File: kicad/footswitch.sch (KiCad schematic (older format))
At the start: 64 parts

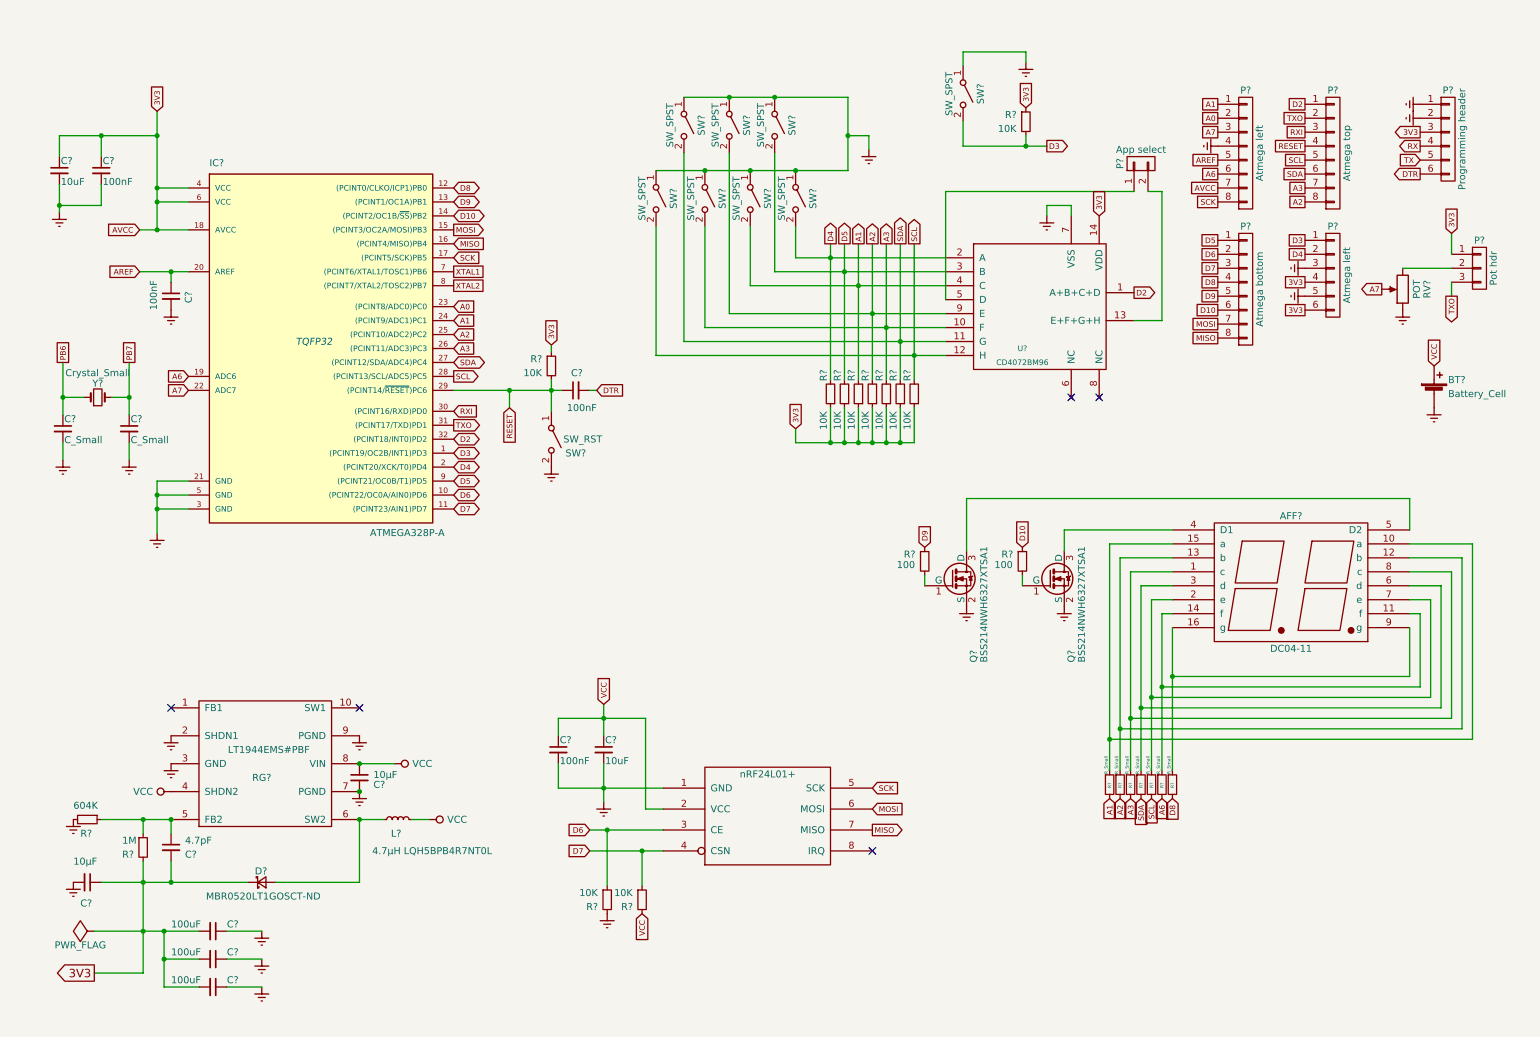
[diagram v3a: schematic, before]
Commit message: Finished schematic
- finished schematic drawing
- added schematic library for ldd-c514ri led display
- added footprint for 100SP4T1B1M1QEH mom-off-mom switch
- annotated footprints for components
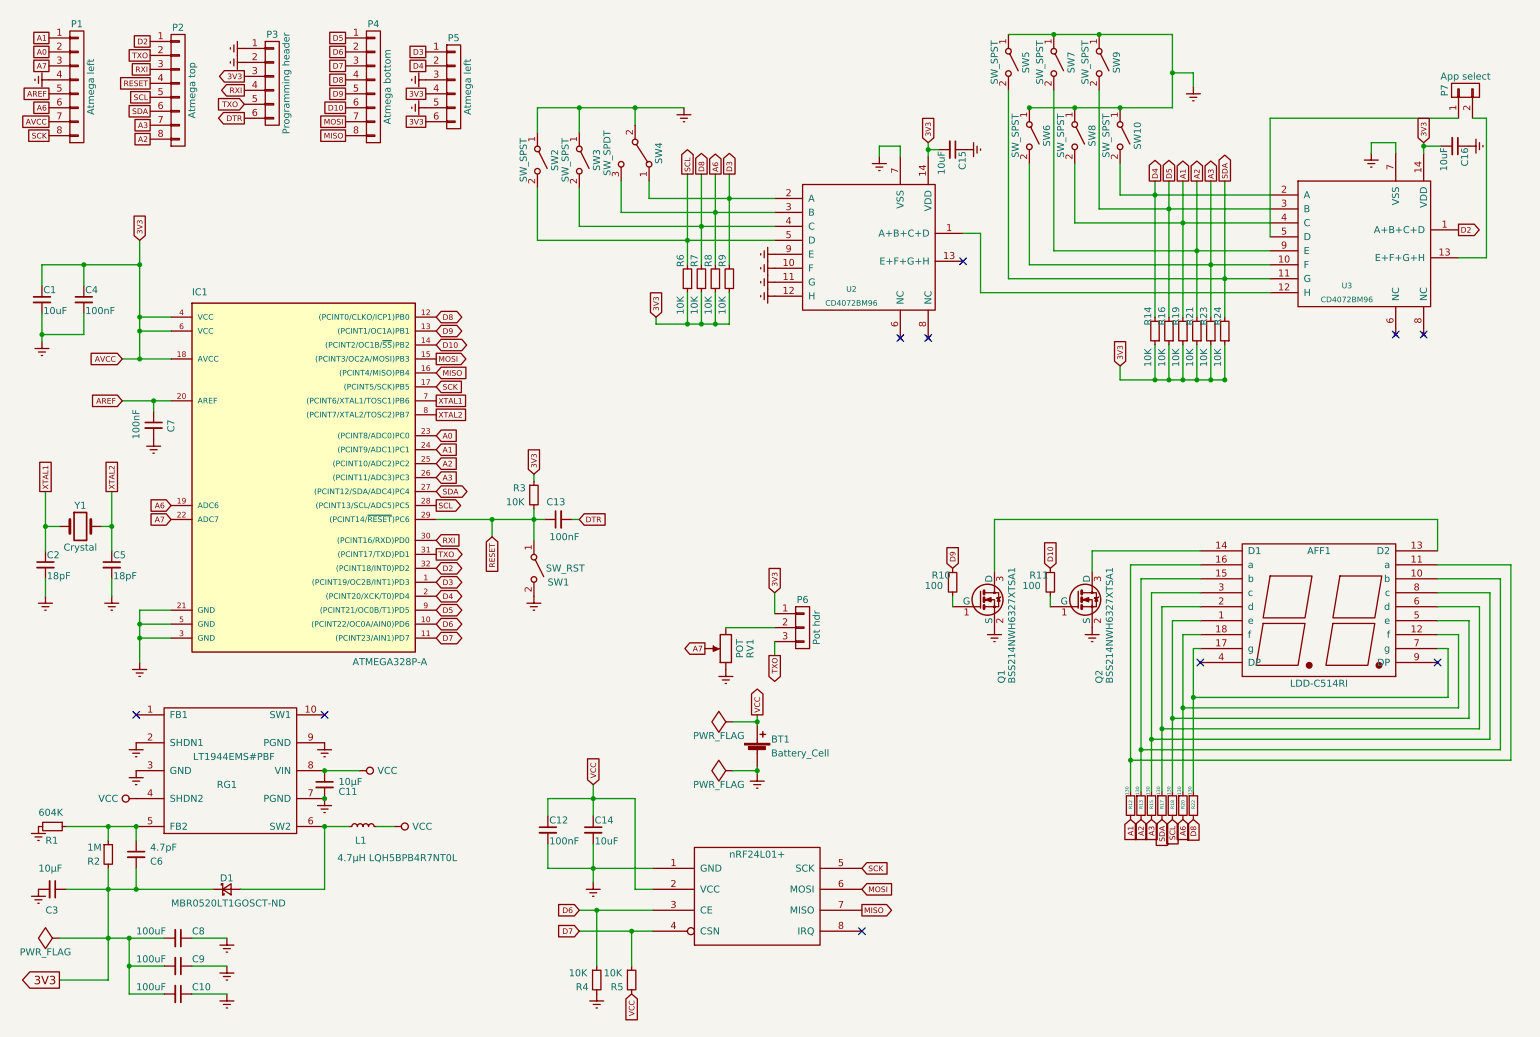
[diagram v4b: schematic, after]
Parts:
- removed AFF?: DC04-11, symbol DC04-11
- removed C? (x2): C_Small, symbol C_Small
- removed R?: 10K, symbol R_Small
- removed R?: 10K, Resistors_SMD:R_0805_HandSoldering, symbol R_Small
- removed Y?: Crystal_Small, symbol Crystal_Small
- added AFF1: LDD-C514RI, Displays_7-Segment:DA56, symbol LDD-C514RI
- added C15, C16: 10uF, Capacitors_SMD:C_1206_HandSoldering, symbol C_Small
- added C2, C5: 18pF, Capacitors_SMD:C_1206_HandSoldering, symbol C_Small
- added R6, R7, R8, R9: 10K, Resistors_SMD:R_1206_HandSoldering, symbol R_Small
- added SW4: SW_SPDT, switches:100SP4T1B1M1QEH, symbol SW_SPDT
- added U2: CD4072BM96, Housings_SOIC:SOIC-14_3.9x8.7mm_Pitch1.27mm, symbol CD4072BM96
- added Y1: Crystal, Crystals:Crystal_SMD_Abracon_ABM3-2pin_5.0x3.2mm_HandSoldering, symbol Crystal
- BT1: renamed from BT?; footprint (none) -> BC2AAPC:BC2AAPC
- C1, C12, C13, C14, C4, C7: renamed from C?; footprint (none) -> Capacitors_SMD:C_1206_HandSoldering
- C11, C3, C6: renamed from C?; footprint Capacitors_SMD:C_0805_HandSoldering -> Capacitors_SMD:C_1206_HandSoldering
- D1: renamed from D?; footprint Diodes_SMD:SOD-123 -> Diodes_SMD:D_SOD-123
- IC1: renamed from IC?; footprint TQFP32 -> Housings_QFP:TQFP-32_7x7mm_Pitch0.8mm
- L1: renamed from L?; footprint (none) -> Inductors:Inductor_Taiyo-Yuden_NR-50xx_HandSoldering
- P1, P2, P4: renamed from P?; footprint (none) -> Pin_Headers:Pin_Header_Straight_1x08_Pitch2.54mm
- P3, P5: renamed from P?; footprint (none) -> Pin_Headers:Pin_Header_Straight_1x06_Pitch2.54mm
- P6: renamed from P?; footprint (none) -> Pin_Headers:Pin_Header_Straight_1x03_Pitch2.54mm
- P7: renamed from P?; footprint (none) -> Pin_Headers:Pin_Header_Straight_1x02_Pitch2.54mm
- Q1, Q2: renamed from Q?; footprint TO_SOT_Packages_SMD:SOT-23 -> TO_SOT_Packages_SMD:SOT-323_SC-70_Handsoldering
- R1, R14, R16, R19, R2, R21, R23, R24, R4, R5: renamed from R?; footprint Resistors_SMD:R_0805_HandSoldering -> Resistors_SMD:R_1206_HandSoldering
- R10, R11, R3: renamed from R?; footprint (none) -> Resistors_SMD:R_1206_HandSoldering
- R12, R13, R15, R17, R18, R20, R22: renamed from R?; value R_Small -> 130; footprint (none) -> Resistors_SMD:R_1206_HandSoldering
- RV1: renamed from RV?; footprint (none) -> Pin_Headers:Pin_Header_Straight_1x03_Pitch2.54mm
- SW1: renamed from SW?; footprint (none) -> Buttons_Switches_SMD:SW_SPST_B3S-1000
- SW10, SW2, SW3, SW5, SW6, SW7, SW8, SW9: renamed from SW?; footprint (none) -> Pin_Headers:Pin_Header_Straight_1x02_Pitch2.54mm
- U1: renamed from U?; footprint MODULE -> mysensors_radios:NRF24L01
- U3: renamed from U?; footprint (none) -> Housings_SOIC:SOIC-14_3.9x8.7mm_Pitch1.27mm
- gave numbers to parts that had none: 4
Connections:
- net RX is gone; now on net RXI: P3.4 (P4)
- net TX is gone; now on net TXO: P3.5 (P5)
- net 3V3: now also C15.2, C16.2, R6.1, R7.1, R8.1, R9.1, U2.14 (VDD)
- net A6: now also R8.2, SW4.3 (C), U2.3 (B)
- net D3: now also R9.2, SW4.1 (A), U2.2 (A); no longer SW3.2 (B)
- net D8: now also SW3.2 (B), R7.2, U2.4 (C)
- net Earth: now also C15.1, C16.1, C2.2, C5.2, SW4.2 (B), U2.10 (F), U2.11 (G), U2.12 (H), U2.7 (VSS), U2.9 (E)
- net SCL: now also R6.2, U2.5 (D); no longer U3.12 (H)
- net XTAL1: now also C2.1, Y1.1
- net XTAL2: now also C5.1, Y1.2
- net at R15.1: now also AFF1.3 (c), AFF1.8 (c)
- net at R12.1: now also AFF1.11 (a), AFF1.16 (a)
- net at R20.1: now also AFF1.12 (f), AFF1.18 (f)
- net at R13.1: now also AFF1.10 (b), AFF1.15 (b)
- net at R22.1: now also AFF1.17 (g), AFF1.7 (g)
- net at R18.1: now also AFF1.1 (e), AFF1.5 (e)
- net at R17.1: now also AFF1.2 (d), AFF1.6 (d)
- net at Q2.3 (D): now also AFF1.14 (D1)
- net at Q1.3 (D): now also AFF1.13 (D2)
- new net: U2.1 (A+B+C+D), U3.12 (H)
- no-connect marks 5 -> 10
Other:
- moved on the sheet: BT1, C1, C10, C11, C12, C13, C14, C3, C4, C6, C7, C8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

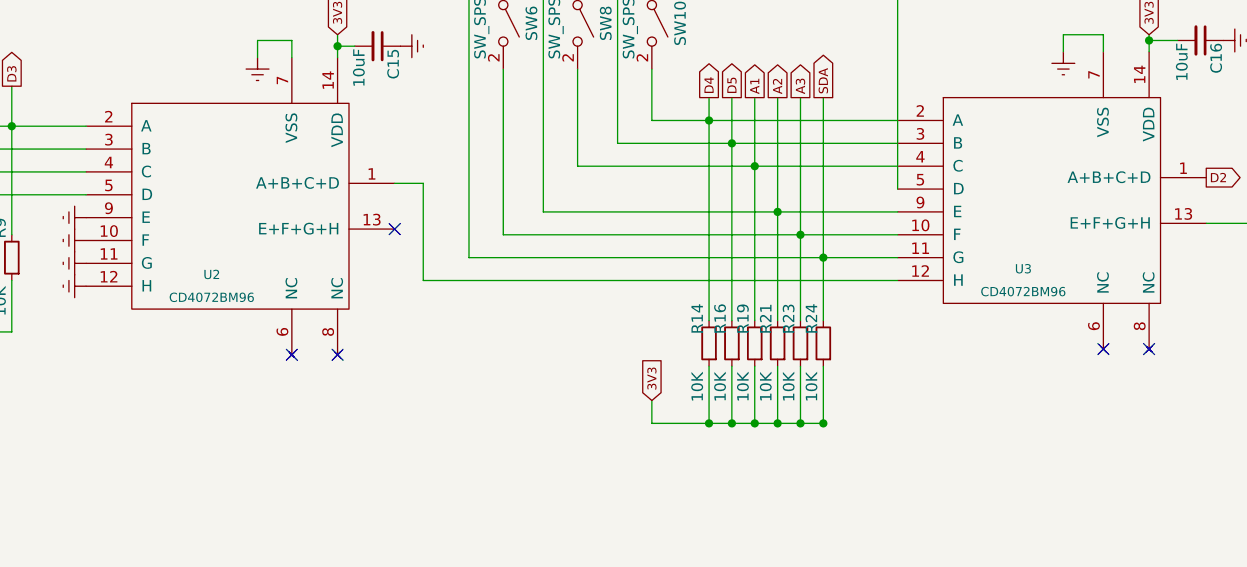
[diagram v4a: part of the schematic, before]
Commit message: Fix CD4072BM96 footprint
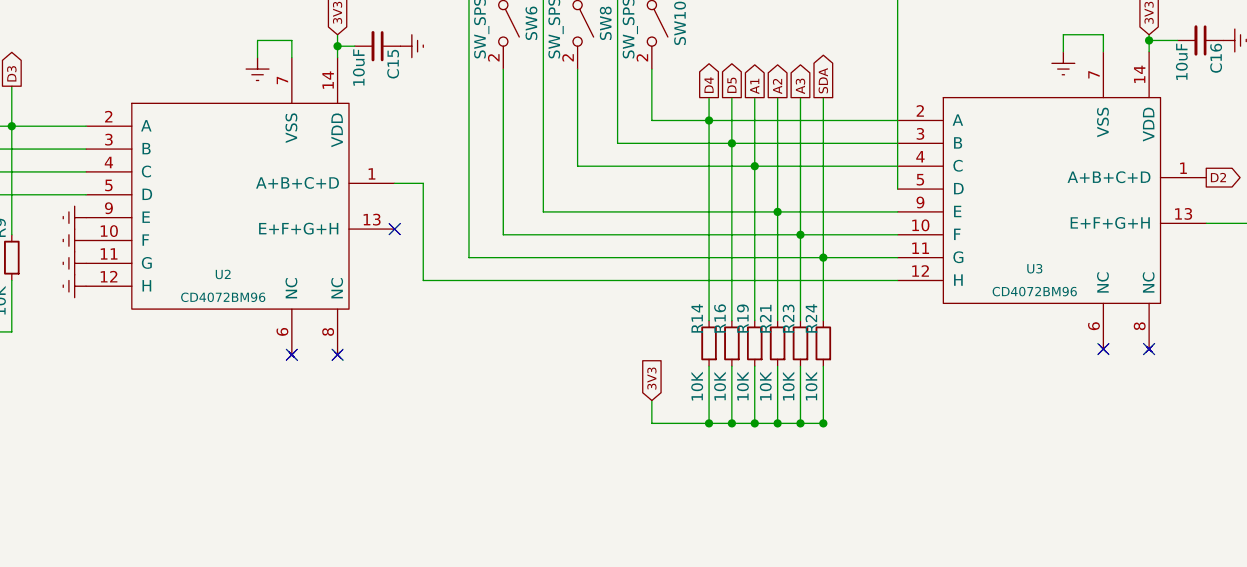
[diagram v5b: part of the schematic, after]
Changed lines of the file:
@@
-$EndComp
-$Comp
-L CD4072BM96 U3
-U 1 1 58EFDB27
-P 10175 2150
-F 0 "U3" H 10025 1850 40  0000 C CNN
-F 1 "CD4072BM96" H 10025 1750 40  0000 C CNN
-F 2 "Housings_SOIC:SOIC-14_3.9x8.7mm_Pitch1.27mm" H 10025 2250 40  0001 C CNN
-F 3 "" H 10025 2250 40  0001 C CNN
-	1    10175 2150
-	1    0    0    -1
 $EndComp
 $Comp
@@
 $EndComp
 $Comp
-L CD4072BM96 U2
-U 1 1 58F11A33
-P 6625 2175
-F 0 "U2" H 6475 1875 40  0000 C CNN
-F 1 "CD4072BM96" H 6475 1775 40  0000 C CNN
-F 2 "Housings_SOIC:SOIC-14_3.9x8.7mm_Pitch1.27mm" H 6475 2275 40  0001 C CNN
-F 3 "" H 6475 2275 40  0001 C CNN
-	1    6625 2175
-	1    0    0    -1
-$EndComp
-$Comp
 L SW_SPDT SW4
 U 1 1 58F1249D
@@
 	1175 4675 1175 4550
 Connection ~ 1175 4175
+$Comp
+L CD4072BM96 U2
+U 1 1 58F385FD
+P 6625 2175
+F 0 "U2" H 6525 1875 40  0000 C CNN
+F 1 "CD4072BM96" H 6525 1775 40  0000 C CNN
+F 2 "Housings_SOIC:SOIC-14_3.9x8.7mm_Pitch1.27mm" H 6475 2275 40  0001 C CNN
+F 3 "" H 6475 2275 40  0001 C CNN
+	1    6625 2175
+	1    0    0    -1
+$EndComp
+$Comp
+L CD4072BM96 U3
+U 1 1 58F38DDC
+P 10175 2150
+F 0 "U3" H 10075 1850 40  0000 C CNN
+F 1 "CD4072BM96" H 10075 1750 40  0000 C CNN
+F 2 "Housings_SOIC:SOIC-14_3.9x8.7mm_Pitch1.27mm" H 10025 2250 40  0001 C CNN
+F 3 "" H 10025 2250 40  0001 C CNN
+	1    10175 2150
+	1    0    0    -1
+$EndComp
 $EndSCHEMATC

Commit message: Fix bugs in schematic; start routing
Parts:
- added R25, R26: 10K, Resistors_SMD:R_1206_HandSoldering, symbol R_Small
- P1: value Atmega left -> Atmega right
- P5: footprint Pin_Headers:Pin_Header_Straight_1x06_Pitch2.54mm -> Pin_Headers:Pin_Header_Straight_1x04_Pitch2.54mm; symbol CONN_01X06 -> CONN_01X04
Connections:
- net 3V3: now also SW10.1 (A), SW2.1 (A), SW3.1 (A), SW4.2 (B), SW5.1 (A), SW6.1 (A), SW7.1 (A), SW8.1 (A), SW9.1 (A); no longer P5.6 (P6), R14.1, R16.1, R19.1, R21.1, R23.1, R24.1, R6.1, R7.1, R8.1, R9.1
- net D10: now also R26.1
- net D9: now also R25.1
- net Earth: now also R14.1, R16.1, R19.1, R21.1, R23.1, R24.1, R6.1, R7.1, R8.1, R9.1, R25.2, R26.2; no longer P5.5 (P5), SW10.1 (A), SW2.1 (A), SW3.1 (A), SW4.2 (B), SW5.1 (A), SW6.1 (A), SW7.1 (A), SW8.1 (A), SW9.1 (A)
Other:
- moved on the sheet: AFF1, BT1, C15, C16, P6, P7, Q1, Q2, R10, R11, R12, R13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

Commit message: Continue routing
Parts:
- BT1: footprint BC2AAPC:BC2AAPC -> Pin_Headers:Pin_Header_Straight_1x02_Pitch2.54mm
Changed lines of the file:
@@
 F 0 "BT1" H 5650 5750 50  0000 L CNN
 F 1 "Battery_Cell" H 5650 5650 50  0000 L CNN
-F 2 "BC2AAPC:BC2AAPC" V 5550 5710 50  0001 C CNN
+F 2 "Pin_Headers:Pin_Header_Straight_1x02_Pitch2.54mm" V 5550 5710 50  0001 C CNN
 F 3 "" V 5550 5710 50  0000 C CNN
 	1    5550 5650
